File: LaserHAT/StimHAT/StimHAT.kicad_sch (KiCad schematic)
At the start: 112 parts, among them J1 GPIO, J10 OLED 0.91 (GND VCC SCL SDA), J101 ELECTRODE E1/E2, J102 B4B-PH-K-S(LF)(SN), J103 5V TO DC-DC POD, J5 GT-USB-7010ASV, J6 BNC TRIGGER IN, J7 BNC STIM OUT, Q3 AP30P30Q, Q4 DMMT5401, Q5 AP30P30Q, SW10 MSK12C02, SW6 TS-1088-AR02016, SW7 SKRHADE010, SW9 TS-1088-AR02016, U1 M24C32-WDW6TP, U101 ISO7741FDBQR, U104 TLV76050DBZR, U105 DAC60501ZDGSR, U106 OPA2192IDGKR, U107 CD74HC4053PWR, U108 DG418DY-T1-E3, U109 ISO1640BDR, U110 TLV1702AIDGKR, U4 MCP1700T-3302E/MB, U5 AP2171W, U6 CH340N, U7 MSPM0G1507SRHBR, U8 74LVC2G17GW

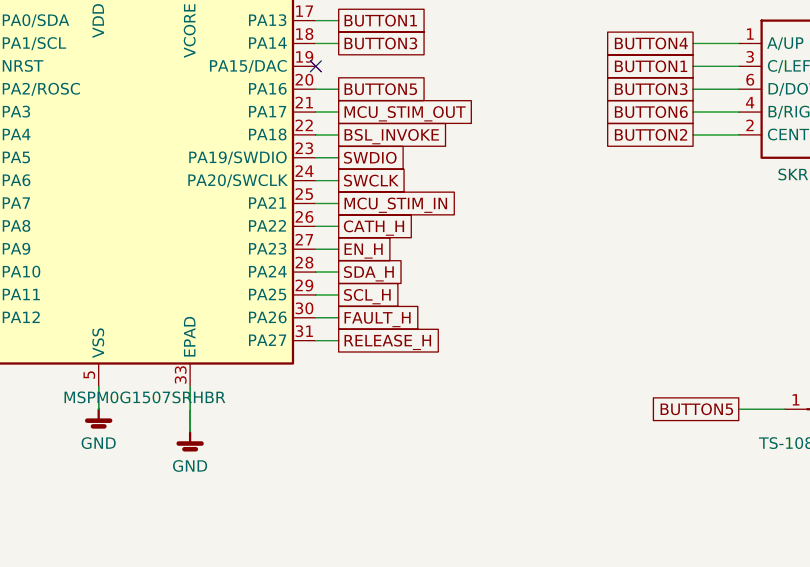
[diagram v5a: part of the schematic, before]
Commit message: StimHAT: U7's east column re-ordered to match the isolator's pin order
At the user's request (routing): top to bottom SCL_H / SDA_H (PA27 / PA26, ADC0 ch 0 / 1) toward
U109, then RELEASE_H, EN_H, CATH_H, FAULT_H (PA25, PA24, PA23, PA22) in U101's HAT-side pin order,
STIM_IN (PA21) at the bottom toward U8.  FAULT_H is now a plain GPIO IRQ pin (the firmware's
fault path already is one; TIMA0's hardware fault inputs are only on PA26 / PA27); for a laser
variant PWM_A on PA24 would be TIMA0_CCP3N or TIMA1_CCP1 against PWM_B on PA23 = TIMA0_CCP3.

Schematic regenerated (netcheck OK, ERC 0), nets pushed into the board with the tracks kept
(path / sync checks 0); the user's SDA_H stub on the old pin 28 was removed.  README pin map
updated.

Co-Authored-By: Claude Fable 5.1 <noreply@anthropic.com>
Claude-Session: https://claude.ai/code/session_015kiXLxnPpBaXdXJu2EMvn7
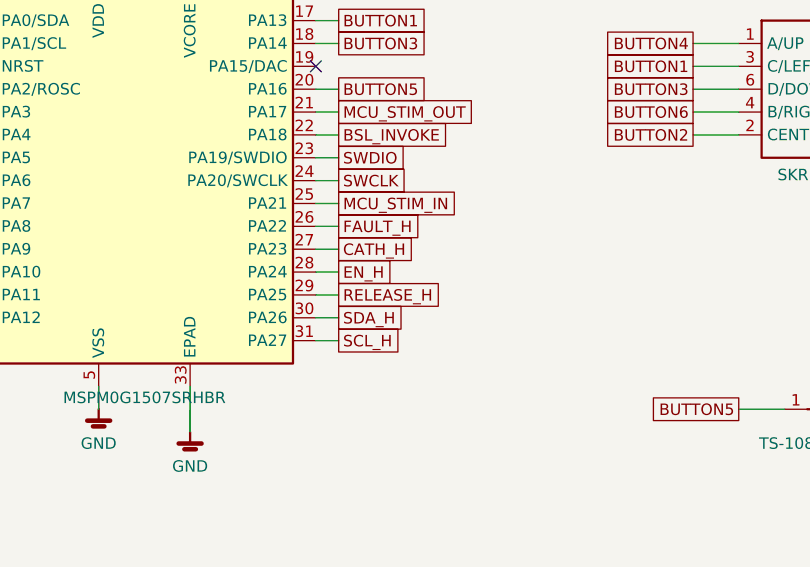
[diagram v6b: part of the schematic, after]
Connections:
- net CATH_H: now also U7.27 (PA23); no longer U7.26 (PA22)
- net EN_H: now also U7.28 (PA24); no longer U7.27 (PA23)
- net FAULT_H: now also U7.26 (PA22); no longer U7.30 (PA26)
- net RELEASE_H: now also U7.29 (PA25); no longer U7.31 (PA27)
- net SCL_H: now also U7.31 (PA27); no longer U7.29 (PA25)
- net SDA_H: now also U7.30 (PA26); no longer U7.28 (PA24)
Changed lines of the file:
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@@
   (global_label "MCU_STIM_IN" (shape passive) (at 407.67 83.82 0) (fields_autoplaced yes) (effects (font (size 1.27 1.27)) (justify left))
     (property "Intersheetrefs" "${INTERSHEET_REFS}" (at 407.67 83.82 0) (effects (font (size 1.27 1.27)) (hide yes))))
-  (global_label "CATH_H" (shape passive) (at 407.67 86.36 0) (fields_autoplaced yes) (effects (font (size 1.27 1.27)) (justify left))
+  (global_label "FAULT_H" (shape passive) (at 407.67 86.36 0) (fields_autoplaced yes) (effects (font (size 1.27 1.27)) (justify left))
     (property "Intersheetrefs" "${INTERSHEET_REFS}" (at 407.67 86.36 0) (effects (font (size 1.27 1.27)) (hide yes))))
-  (global_label "EN_H" (shape passive) (at 407.67 88.9 0) (fields_autoplaced yes) (effects (font (size 1.27 1.27)) (justify left))
+  (global_label "CATH_H" (shape passive) (at 407.67 88.9 0) (fields_autoplaced yes) (effects (font (size 1.27 1.27)) (justify left))
     (property "Intersheetrefs" "${INTERSHEET_REFS}" (at 407.67 88.9 0) (effects (font (size 1.27 1.27)) (hide yes))))
-  (global_label "SDA_H" (shape passive) (at 407.67 91.44 0) (fields_autoplaced yes) (effects (font (size 1.27 1.27)) (justify left))
+  (global_label "EN_H" (shape passive) (at 407.67 91.44 0) (fields_autoplaced yes) (effects (font (size 1.27 1.27)) (justify left))
     (property "Intersheetrefs" "${INTERSHEET_REFS}" (at 407.67 91.44 0) (effects (font (size 1.27 1.27)) (hide yes))))
-  (global_label "SCL_H" (shape passive) (at 407.67 93.98 0) (fields_autoplaced yes) (effects (font (size 1.27 1.27)) (justify left))
+  (global_label "RELEASE_H" (shape passive) (at 407.67 93.98 0) (fields_autoplaced yes) (effects (font (size 1.27 1.27)) (justify left))
     (property "Intersheetrefs" "${INTERSHEET_REFS}" (at 407.67 93.98 0) (effects (font (size 1.27 1.27)) (hide yes))))
-  (global_label "FAULT_H" (shape passive) (at 407.67 96.52 0) (fields_autoplaced yes) (effects (font (size 1.27 1.27)) (justify left))
+  (global_label "SDA_H" (shape passive) (at 407.67 96.52 0) (fields_autoplaced yes) (effects (font (size 1.27 1.27)) (justify left))
     (property "Intersheetrefs" "${INTERSHEET_REFS}" (at 407.67 96.52 0) (effects (font (size 1.27 1.27)) (hide yes))))
-  (global_label "RELEASE_H" (shape passive) (at 407.67 99.06 0) (fields_autoplaced yes) (effects (font (size 1.27 1.27)) (justify left))
+  (global_label "SCL_H" (shape passive) (at 407.67 99.06 0) (fields_autoplaced yes) (effects (font (size 1.27 1.27)) (justify left))
     (property "Intersheetrefs" "${INTERSHEET_REFS}" (at 407.67 99.06 0) (effects (font (size 1.27 1.27)) (hide yes))))
   (symbol (lib_id "stimhat:R") (at 274.32 101.6 0) (unit 1) (exclude_from_sim no) (in_bom yes) (on_board yes) (dnp no)

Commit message: StimHAT: header pins and joystick fan-out re-mapped for routing
Pi header (user's request): PI_TRIGGER -> GPIO18 (pin 12), MCU_PWR_EN -> GPIO10 (pin 19),
NRST -> GPIO9 (pin 21), all in the west half above U7; pins 11 / 13 / 15 are bonnet buttons and
24 / 26 pull up at boot, so NRST takes 21.  Pi side: LASERHAT_NRST_PIN=9 LASERHAT_POWER_PIN=10
LASERHAT_TRIGGER_PIN=18, brokerd --gpio-pin 18.

U7: LED_MCU 9 -> 10 (PA6, frees the PI_RXD / PI_TXD via spot), buttons on 11 / 16 / 17 / 18 / 19
(PA7 / 12 / 13 / 14 / 15) as a 45-degree fan to SW7 in its pad order, FIRE stays on 20.  SW7 at
the user's 135-degree rotation: contact A (pad 1) = down, B (4) = left, C (3) = right, D (6) = up,
nets re-wired to match.  The partly routed BUTTON1/2/3/4/6 copper was ripped (BUTTON5 kept), the
LED's via re-hooked from pin 10.

Schematic regenerated (netcheck OK, ERC 0), nets pushed into the board with the tracks kept
(path / sync checks 0), DRC 0 errors, 49 open connections.  README and placement table updated.

Co-Authored-By: Claude Fable 5.1 <noreply@anthropic.com>
Claude-Session: https://claude.ai/code/session_015kiXLxnPpBaXdXJu2EMvn7
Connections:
- net BUTTON1: now also SW7.4 (B/RIGHT), U7.11 (PA7); no longer SW7.3 (C/LEFT), U7.17 (PA13)
- net BUTTON2: now also U7.18 (PA14); no longer U7.16 (PA12)
- net BUTTON3: now also SW7.1 (A/UP), U7.19 (PA15/DAC); no longer SW7.6 (D/DOWN), U7.18 (PA14)
- net BUTTON4: now also SW7.6 (D/DOWN), U7.16 (PA12); no longer SW7.1 (A/UP), U7.10 (PA6)
- net BUTTON6: now also SW7.3 (C/LEFT), U7.17 (PA13); no longer SW7.4 (B/RIGHT), U7.11 (PA7)
- net LED_MCU: now also U7.10 (PA6); no longer U7.9 (PA5)
- net MCU_PWR_EN: now also J1.19 (GPIO10); no longer J1.12 (GPIO18)
- net NRST: now also J1.21 (GPIO9); no longer J1.36 (GPIO16)
- net PI_TRIGGER: now also J1.12 (GPIO18); no longer J1.19 (GPIO10)
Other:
- note added: "Module lines from the Rev 2 J8 / J9 pins: PA6 FAULT_H, PA7 EN_H, PA12 CATH_H, PA15 RELEASE_H, PA17 SDA_H, PA22 SCL_H (StimHAT: see the README's pin map). Joystick SW7 (SKRHADE010, mounted at 135 deg): up PA12,"
- note added: "down PA15, centre PA14, left PA7 (BACK), right PA13 (BUTTON6); FIRE SW9 PA16; LED PA6; all active low. J10: unpopulated socket for a 0.91 in I2C OLED instead of the bonnet."
- note removed: "Module lines from the Rev 2 J8 / J9 pins: PA6 FAULT_H, PA7 EN_H, PA12 CATH_H, PA15 RELEASE_H, PA17 SDA_H, PA22 SCL_H (StimHAT: see the README's pin map). Joystick SW7 (SKRHADE010): up PA13,"
- note removed: "down PA16, centre PA14, left PA21 (BACK), right PA3 (BUTTON6, new); FIRE SW9 PA23; all active low. J10: unpopulated socket for a 0.91 in I2C OLED instead of the bonnet."

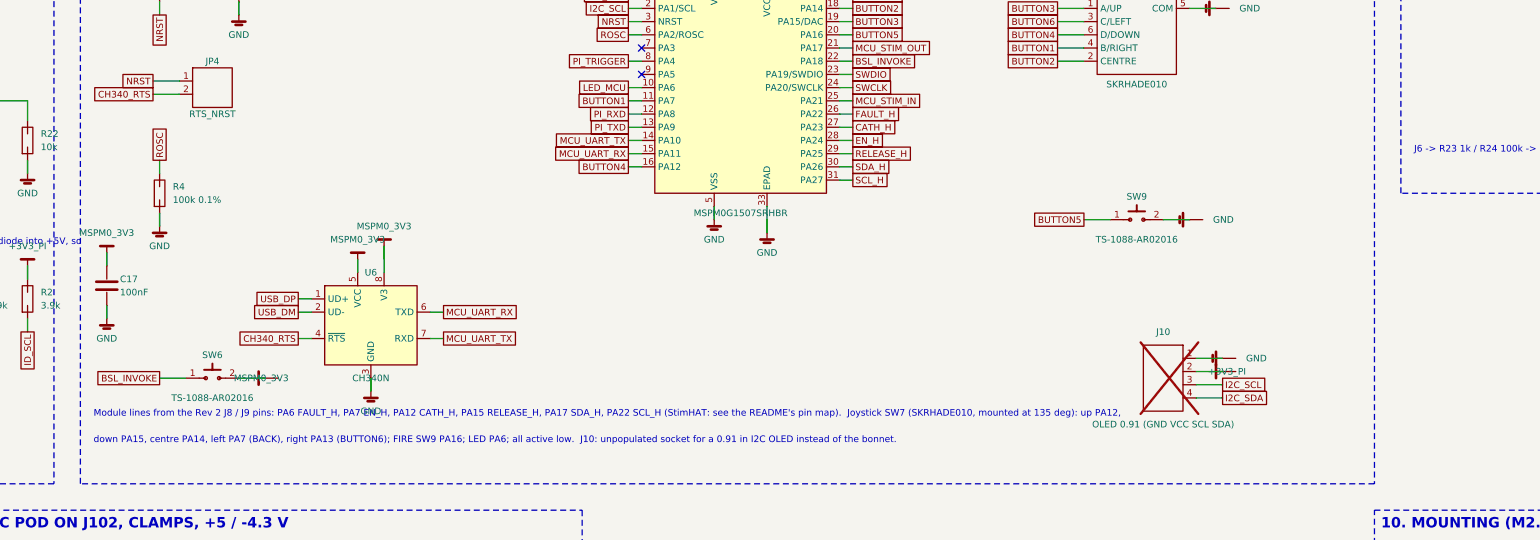
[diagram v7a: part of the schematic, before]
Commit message: StimHAT: BUTTON1 / BUTTON4 swapped on U7 (pins 16 / 11) for the user's routing
U7 pin 11 (PA7) = BUTTON4 (up), pin 16 (PA12) = BUTTON1 (left / BACK); the joystick pads are
unchanged.  The user-routed copper on both pins was re-labelled to the new nets and the 0.75 mm
gap on BUTTON1 at x 12.0 closed.  LED_MCU stays on pin 10.  Schematic regenerated (ERC 0), nets
pushed into the board with the tracks kept, DRC 0 errors, 15 open connections.

Co-Authored-By: Claude Fable 5.1 <noreply@anthropic.com>
Claude-Session: https://claude.ai/code/session_015kiXLxnPpBaXdXJu2EMvn7
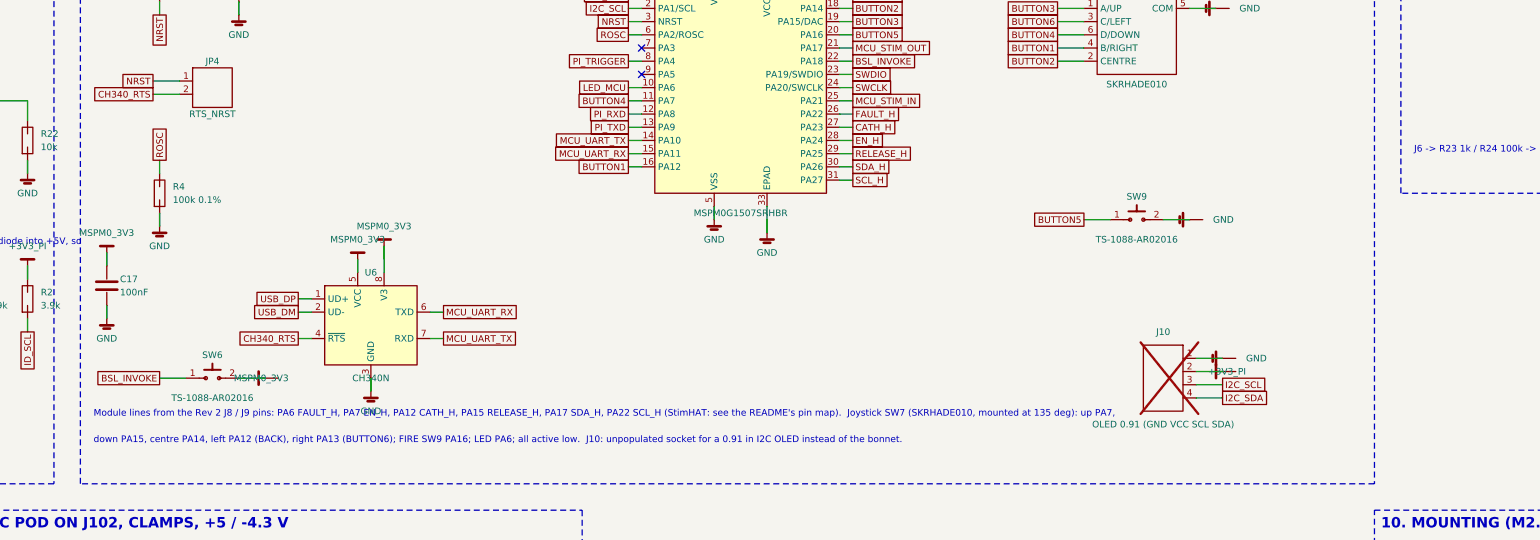
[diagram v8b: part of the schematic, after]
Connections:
- net BUTTON1: now also U7.16 (PA12); no longer U7.11 (PA7)
- net BUTTON4: now also U7.11 (PA7); no longer U7.16 (PA12)
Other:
- note added: "Module lines from the Rev 2 J8 / J9 pins: PA6 FAULT_H, PA7 EN_H, PA12 CATH_H, PA15 RELEASE_H, PA17 SDA_H, PA22 SCL_H (StimHAT: see the README's pin map). Joystick SW7 (SKRHADE010, mounted at 135 deg): up PA7,"
- note added: "down PA15, centre PA14, left PA12 (BACK), right PA13 (BUTTON6); FIRE SW9 PA16; LED PA6; all active low. J10: unpopulated socket for a 0.91 in I2C OLED instead of the bonnet."
- note removed: "Module lines from the Rev 2 J8 / J9 pins: PA6 FAULT_H, PA7 EN_H, PA12 CATH_H, PA15 RELEASE_H, PA17 SDA_H, PA22 SCL_H (StimHAT: see the README's pin map). Joystick SW7 (SKRHADE010, mounted at 135 deg): up PA12,"
- note removed: "down PA15, centre PA14, left PA7 (BACK), right PA13 (BUTTON6); FIRE SW9 PA16; LED PA6; all active low. J10: unpopulated socket for a 0.91 in I2C OLED instead of the bonnet."
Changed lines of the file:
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@@
   (global_label "LED_MCU" (shape passive) (at 364.49 81.28 180) (fields_autoplaced yes) (effects (font (size 1.27 1.27)) (justify right))
     (property "Intersheetrefs" "${INTERSHEET_REFS}" (at 364.49 81.28 0) (effects (font (size 1.27 1.27)) (hide yes))))
-  (global_label "BUTTON1" (shape passive) (at 364.49 83.82 180) (fields_autoplaced yes) (effects (font (size 1.27 1.27)) (justify right))
+  (global_label "BUTTON4" (shape passive) (at 364.49 83.82 180) (fields_autoplaced yes) (effects (font (size 1.27 1.27)) (justify right))
     (property "Intersheetrefs" "${INTERSHEET_REFS}" (at 364.49 83.82 0) (effects (font (size 1.27 1.27)) (hide yes))))
   (global_label "PI_RXD" (shape passive) (at 364.49 86.36 180) (fields_autoplaced yes) (effects (font (size 1.27 1.27)) (justify right))
@@
   (global_label "MCU_UART_RX" (shape passive) (at 364.49 93.98 180) (fields_autoplaced yes) (effects (font (size 1.27 1.27)) (justify right))
     (property "Intersheetrefs" "${INTERSHEET_REFS}" (at 364.49 93.98 0) (effects (font (size 1.27 1.27)) (hide yes))))
-  (global_label "BUTTON4" (shape passive) (at 364.49 96.52 180) (fields_autoplaced yes) (effects (font (size 1.27 1.27)) (justify right))
+  (global_label "BUTTON1" (shape passive) (at 364.49 96.52 180) (fields_autoplaced yes) (effects (font (size 1.27 1.27)) (justify right))
     (property "Intersheetrefs" "${INTERSHEET_REFS}" (at 364.49 96.52 0) (effects (font (size 1.27 1.27)) (hide yes))))
   (global_label "BUTTON6" (shape passive) (at 407.67 63.5 0) (fields_autoplaced yes) (effects (font (size 1.27 1.27)) (justify left))
@@
   (global_label "I2C_SDA" (shape passive) (at 478.79 140.97 0) (fields_autoplaced yes) (effects (font (size 1.27 1.27)) (justify left))
     (property "Intersheetrefs" "${INTERSHEET_REFS}" (at 478.79 140.97 0) (effects (font (size 1.27 1.27)) (hide yes))))
-  (text "Module lines from the Rev 2 J8 / J9 pins: PA6 FAULT_H, PA7 EN_H, PA12 CATH_H, PA15 RELEASE_H, PA17 SDA_H, PA22 SCL_H (StimHAT: see the README's pin map).  Joystick SW7 (SKRHADE010, mounted at 135 deg): up PA12," (exclude_from_sim no) (at 261.62 144.78 0) (effects (font (size 1.27 1.27)) (justify left bottom)))
-  (text "down PA15, centre PA14, left PA7 (BACK), right PA13 (BUTTON6); FIRE SW9 PA16; LED PA6; all active low.  J10: unpopulated socket for a 0.91 in I2C OLED instead of the bonnet." (exclude_from_sim no) (at 261.62 149.86 0) (effects (font (size 1.27 1.27)) (justify left bottom)))
+  (text "Module lines from the Rev 2 J8 / J9 pins: PA6 FAULT_H, PA7 EN_H, PA12 CATH_H, PA15 RELEASE_H, PA17 SDA_H, PA22 SCL_H (StimHAT: see the README's pin map).  Joystick SW7 (SKRHADE010, mounted at 135 deg): up PA7," (exclude_from_sim no) (at 261.62 144.78 0) (effects (font (size 1.27 1.27)) (justify left bottom)))
+  (text "down PA15, centre PA14, left PA12 (BACK), right PA13 (BUTTON6); FIRE SW9 PA16; LED PA6; all active low.  J10: unpopulated socket for a 0.91 in I2C OLED instead of the bonnet." (exclude_from_sim no) (at 261.62 149.86 0) (effects (font (size 1.27 1.27)) (justify left bottom)))
   (rectangle (start 513.08 20.32) (end 640.08 101.6) (stroke (width 0.2) (type dash)) (fill (type none)))
   (text "3. BNC TRIGGER IN / STIM OUT (74LVC2G17 buffers)" (exclude_from_sim no) (at 514.35 24.13 0) (effects (font (size 2.0 2.0) (bold yes)) (justify left bottom)))
